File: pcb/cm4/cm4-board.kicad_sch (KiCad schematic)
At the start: 9 parts, among them J201 DF40C-100DS-0.4V_51_, J202 DF40C-100DS-0.4V_51_, U201 SN74LV1T34DBV

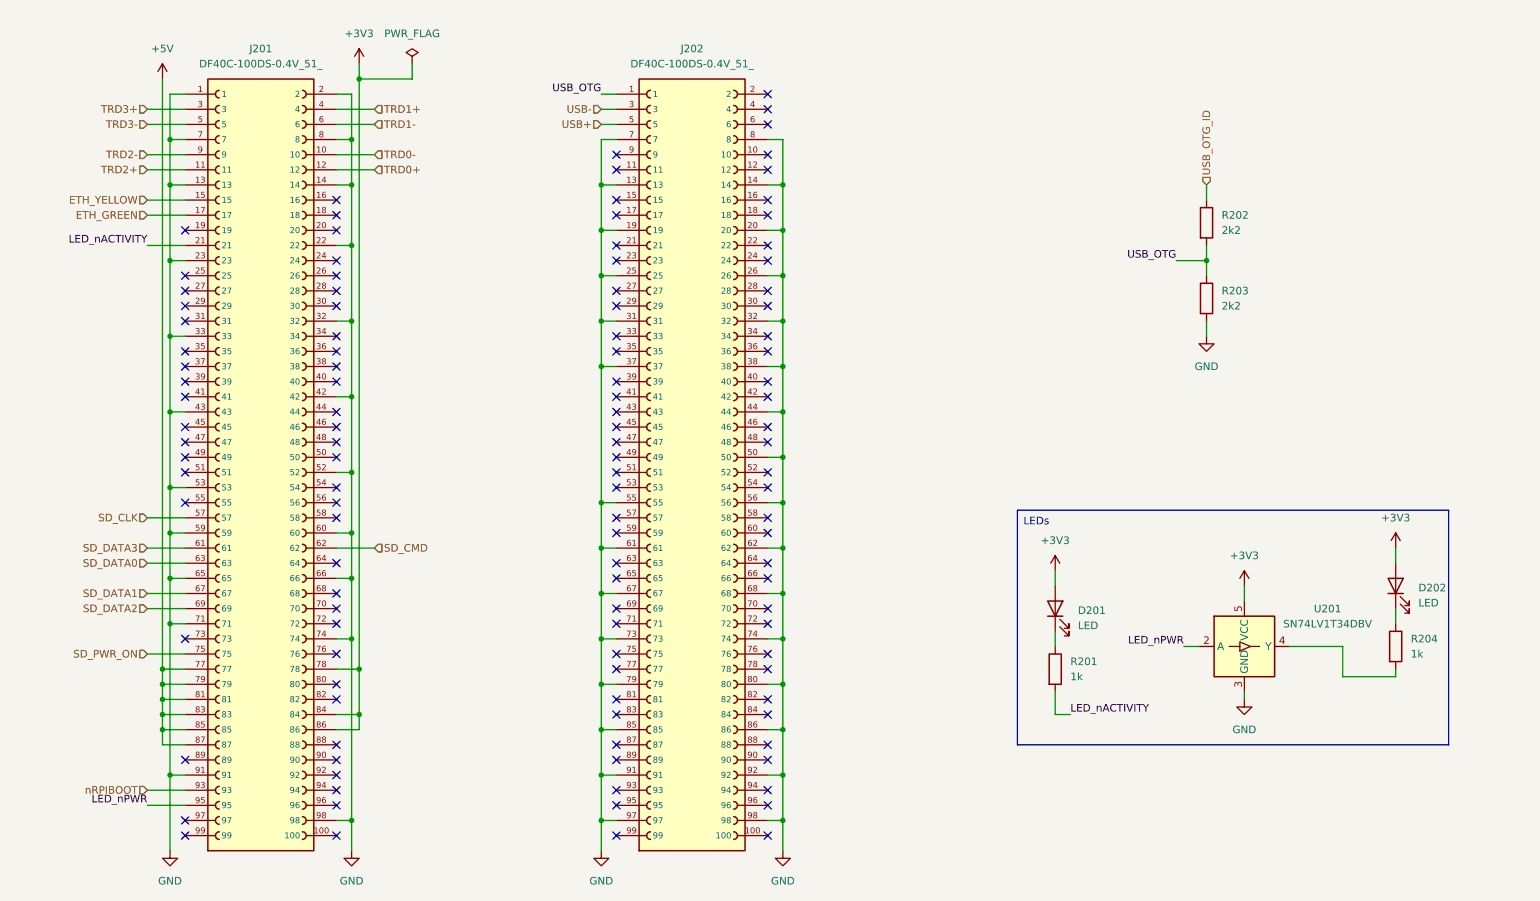
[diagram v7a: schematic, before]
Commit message: add i2c
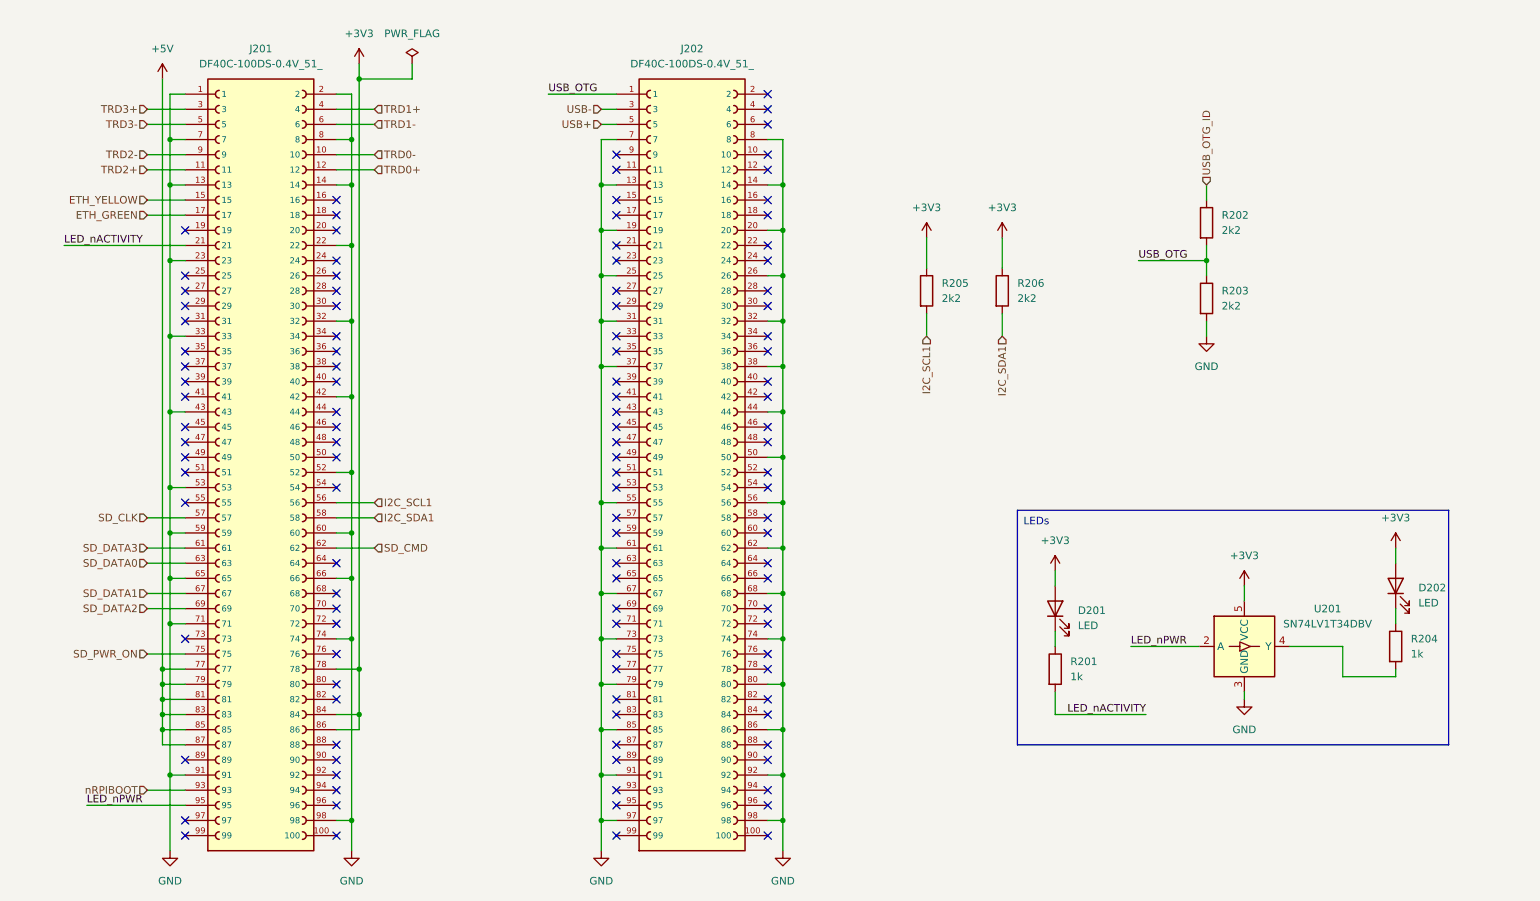
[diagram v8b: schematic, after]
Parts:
- added R205, R206: 2k2, Resistor_SMD:R_0805_2012Metric, symbol Device:R
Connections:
- net +3V3: now also R205.1, R206.1
- net I2C_SCL1: now reaches J201.56
- net I2C_SCL1: now also R205.2
- net I2C_SDA1: now reaches J201.58
- net I2C_SDA1: now also R206.2
- no-connect marks 116 -> 114
